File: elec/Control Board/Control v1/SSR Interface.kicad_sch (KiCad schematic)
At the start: 0 parts

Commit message: added labels for heiarchy sheets, and first pass on basic control interface circuits
Signed-off-by: lokimetasmith <lokimail@gmail.com>
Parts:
- added Q1: BC818, Package_TO_SOT_SMD:SOT-23, symbol Transistor_BJT:BC818
- added R1: R, symbol Device:R
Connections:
- new net: Q1.1 (B), R1.2
- new net +3.3V: Q1.3 (C)
- new net Heater: R1.1
- new net Heater_SSR: Q1.2 (E)
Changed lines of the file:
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@@
 (kicad_sch (version 20230121) (generator eeschema)
   (paper "A4")
+  (wire (pts (xy 59.69 62.23) (xy 68.58 62.23))
+    (stroke (width 0) (type default))
+  )
+  (wire (pts (xy 91.44 67.31) (xy 91.44 76.2))
+    (stroke (width 0) (type default))
+  )
+  (wire (pts (xy 76.2 62.23) (xy 83.82 62.23))
+    (stroke (width 0) (type default))
+  )
+  (wire (pts (xy 91.44 45.72) (xy 91.44 57.15))
+    (stroke (width 0) (type default))
+  )
+  (hierarchical_label "Heater" (shape input) (at 59.69 62.23 180) (fields_autoplaced)
+    (effects (font (size 1.27 1.27)) (justify right))
+  )
+  (hierarchical_label "Heater_SSR" (shape input) (at 91.44 76.2 270) (fields_autoplaced)
+    (effects (font (size 1.27 1.27)) (justify right))
+  )
+  (symbol (lib_id "power:+3.3V") (at 91.44 45.72 0) (unit 1)
+    (in_bom yes) (on_board yes) (dnp no) (fields_autoplaced)
+    (property "Reference" "#PWR01" (at 91.44 49.53 0)
+      (effects (font (size 1.27 1.27)) hide)
+    )
+    (property "Value" "+3.3V" (at 91.44 41.91 0)
+      (effects (font (size 1.27 1.27)))
+    )
+    (property "Footprint" "" (at 91.44 45.72 0)
+      (effects (font (size 1.27 1.27)) hide)
+    )
+    (property "Datasheet" "" (at 91.44 45.72 0)
+      (effects (font (size 1.27 1.27)) hide)
+    )
+    (pin "1")
+    (instances
+      (project "Control v1"
+        (path "/c68c9deb-8d4d-42f0-adf8-4d3022f4ee59/4a4acea4-18ba-4b87-a925-0ac6ac8c0a01"
+          (reference "#PWR01") (unit 1)
+        )
+      )
+    )
+  )
+  (symbol (lib_id "Device:R") (at 72.39 62.23 90) (unit 1)
+    (in_bom yes) (on_board yes) (dnp no) (fields_autoplaced)
+    (property "Reference" "R1" (at 72.39 57.15 90)
+      (effects (font (size 1.27 1.27)))
+    )
+    (property "Value" "R" (at 72.39 59.69 90)
+      (effects (font (size 1.27 1.27)))
+    )
+    (property "Footprint" "" (at 72.39 64.008 90)
+      (effects (font (size 1.27 1.27)) hide)
+    )
+    (property "Datasheet" "~" (at 72.39 62.23 0)
+      (effects (font (size 1.27 1.27)) hide)
+    )
+    (pin "1")
+    (pin "2")
+    (instances
+      (project "Control v1"
+        (path "/c68c9deb-8d4d-42f0-adf8-4d3022f4ee59/4a4acea4-18ba-4b87-a925-0ac6ac8c0a01"
+          (reference "R1") (unit 1)
+        )
+      )
+    )
+  )
+  (symbol (lib_id "Transistor_BJT:BC818") (at 88.9 62.23 0) (unit 1)
+    (in_bom yes) (on_board yes) (dnp no) (fields_autoplaced)
+    (property "Reference" "Q1" (at 93.98 61.595 0)
+      (effects (font (size 1.27 1.27)) (justify left))
+    )
+    (property "Value" "BC818" (at 93.98 64.135 0)
+      (effects (font (size 1.27 1.27)) (justify left))
+    )
+    (property "Footprint" "Package_TO_SOT_SMD:SOT-23" (at 93.98 64.135 0)
+      (effects (font (size 1.27 1.27) italic) (justify left) hide)
+    )
+    (property "Datasheet" "https://www.onsemi.com/pub/Collateral/BC818-D.pdf" (at 88.9 62.23 0)
+      (effects (font (size 1.27 1.27)) (justify left) hide)
+    )
+    (pin "1")
+    (pin "2")
+    (pin "3")
+    (instances
+      (project "Control v1"
+        (path "/c68c9deb-8d4d-42f0-adf8-4d3022f4ee59/4a4acea4-18ba-4b87-a925-0ac6ac8c0a01"
+          (reference "Q1") (unit 1)
+        )
+      )
+    )
+  )
 )

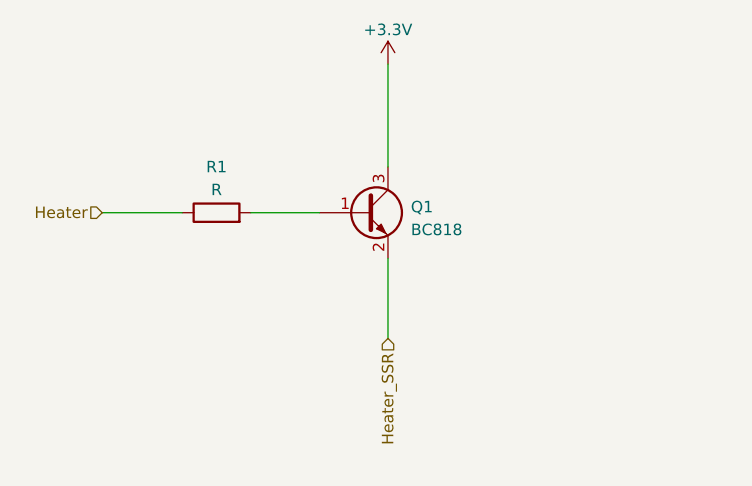
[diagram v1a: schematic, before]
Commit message: Add fan circuits. Add thermocouple interface circuits.
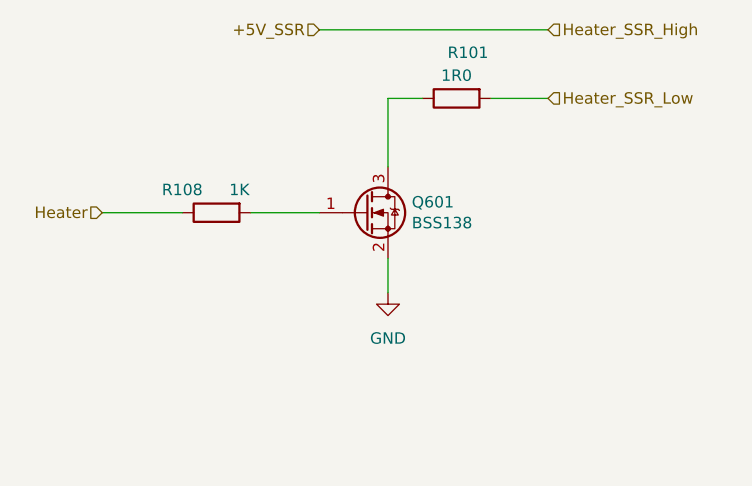
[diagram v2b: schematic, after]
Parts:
- removed Q1: BC818, Package_TO_SOT_SMD:SOT-23, symbol Transistor_BJT:BC818
- removed R1: R, symbol Device:R
- added Q601: BSS138, Package_TO_SOT_SMD:SOT-23, symbol Transistor_FET:BSS138
- added R101: 1R0, Resistor_SMD:R_0603_1608Metric_Pad0.98x0.95mm_HandSolder, symbol Device:R
- added R108: 1K, Resistor_SMD:R_0603_1608Metric_Pad0.98x0.95mm_HandSolder, symbol Device:R
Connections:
- net Heater: now also R108.1
- new net: Q601.1 (G), R108.2
- new net: Q601.3 (D), R101.1
- new net GND: Q601.2 (S)
- new net Heater_SSR_Low: R101.2

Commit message: Move some components for rough placement.
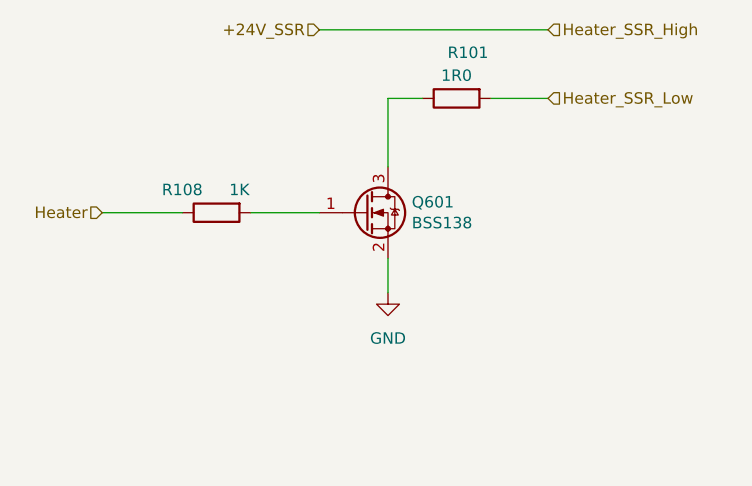
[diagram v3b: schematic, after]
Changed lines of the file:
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@@
     (effects (font (size 1.27 1.27)) (justify right))
   )
-  (hierarchical_label "+5V_SSR" (shape input) (at 83.82 41.91 180) (fields_autoplaced)
+  (hierarchical_label "+24V_SSR" (shape input) (at 83.82 41.91 180) (fields_autoplaced)
     (effects (font (size 1.27 1.27)) (justify right))
   )
@@
         )
         (path "/c68c9deb-8d4d-42f0-adf8-4d3022f4ee59/4a4acea4-18ba-4b87-a925-0ac6ac8c0a01"
-          (reference "Q3") (unit 1)
+          (reference "Q4") (unit 1)
         )
       )
@@
         )
         (path "/c68c9deb-8d4d-42f0-adf8-4d3022f4ee59/4a4acea4-18ba-4b87-a925-0ac6ac8c0a01"
-          (reference "#PWR01") (unit 1)
+          (reference "#PWR045") (unit 1)
         )
       )
@@
         )
         (path "/c68c9deb-8d4d-42f0-adf8-4d3022f4ee59/4a4acea4-18ba-4b87-a925-0ac6ac8c0a01"
-          (reference "R1") (unit 1)
+          (reference "R23") (unit 1)
         )
       )
@@
         )
         (path "/c68c9deb-8d4d-42f0-adf8-4d3022f4ee59/4a4acea4-18ba-4b87-a925-0ac6ac8c0a01"
-          (reference "R16") (unit 1)
+          (reference "R22") (unit 1)
         )
       )
